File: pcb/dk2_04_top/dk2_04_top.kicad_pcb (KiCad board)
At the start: 2 copper layers, 120 x 108 mm, 112 parts, among them J1 Conn_01x20_Socket, J10 Sync_Out, J11 Euro_Out_2, J12 CV_In_1, J13 CV_In_2, J14 CV_In_3, J15 CV_In_4, J16 Conn_01x05_Pin, J2 Trigger_Out_1, J3 Trigger_Out_2, J4 Sync_In, J5 Euro_Out_1, J6 Micro_SD_Card, J7 Conn_01x16_Socket, J8 Trigger_Out_3, J9 Trigger_Out_4, SW1 SW_Push, SW10 SW_Push, SW11 SW_Push, SW12 SW_Push, SW13 SW_Push, SW14 SW_Push, SW15 SW_Push, SW16 SW_Push, SW17 SW_Push, SW18 SW_Push, SW19 SW_Push, SW2 SW_Push, SW3 SW_Push, SW4 SW_Push, SW5 SW_Push, SW6 SW_Push, SW7 SW_Push, SW8 SW_Push, SW9 SW_Push, U1 74HC595, U10 74HC165, U2 74HC595, U3 CA56-12EWA, U4 74HC165, U5 74HC165, U6 74HC4051, U7 MCP6002-xSN, U8 MCP6002-xSN, U9 74HC4051

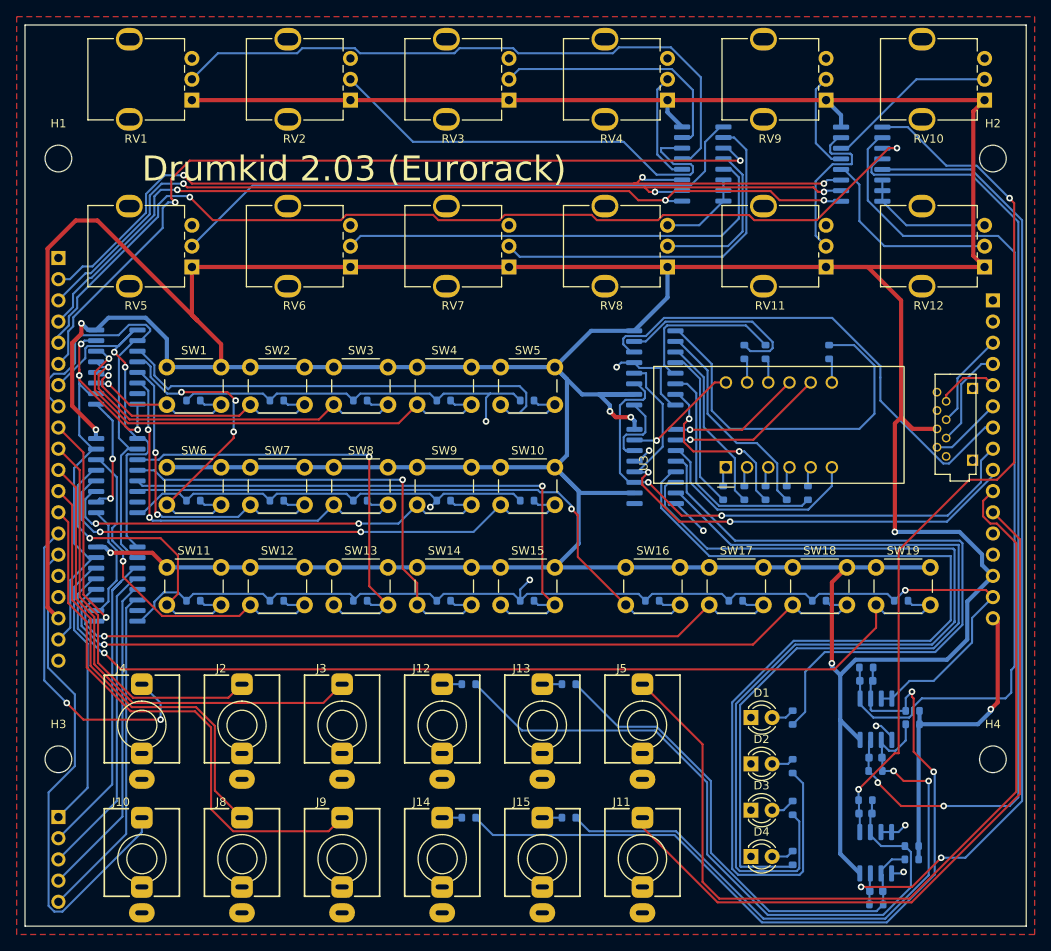
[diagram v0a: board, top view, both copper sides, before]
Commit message: rejigged top board, smaller connectors
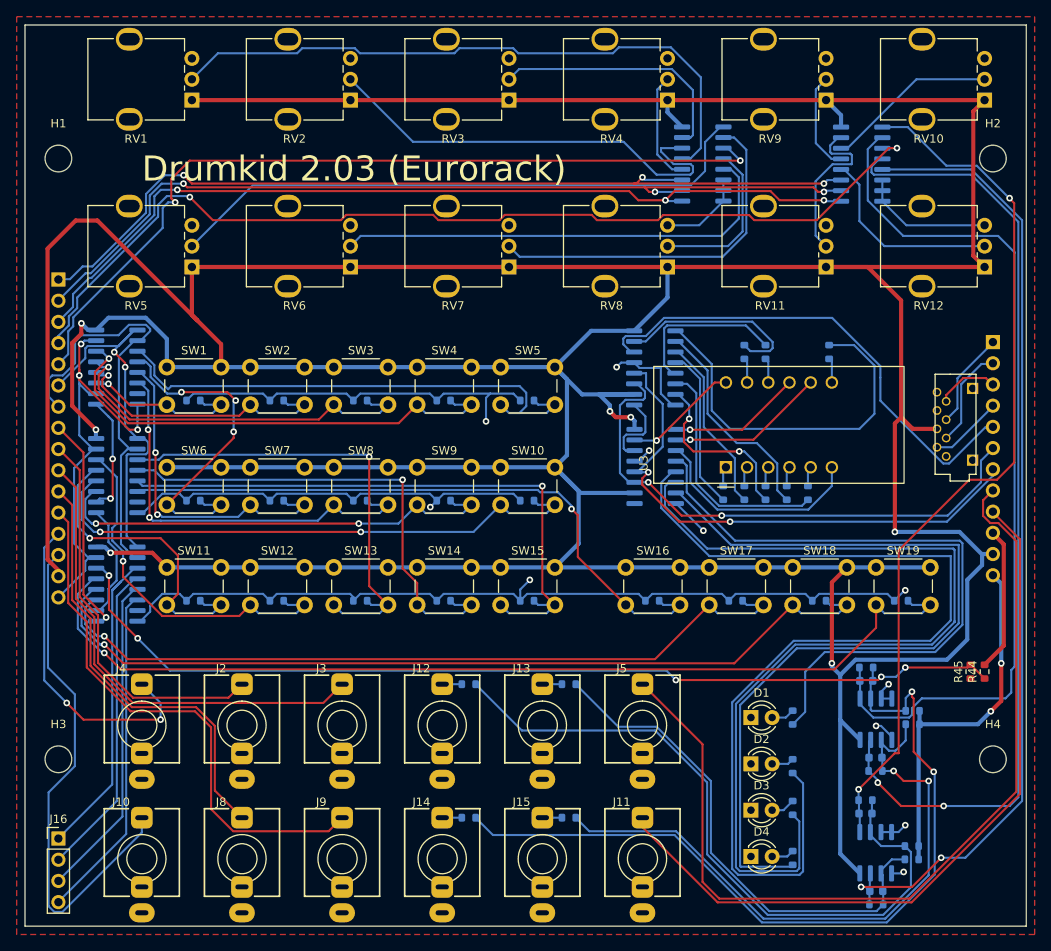
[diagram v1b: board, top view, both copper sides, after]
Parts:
- added R44: 330k, Resistor_SMD:R_0603_1608Metric, F.Cu at (185.0, 117.5)
- added R45: 100k, Resistor_SMD:R_0603_1608Metric, F.Cu at (183.3, 117.5)
- J1: value Conn_01x20_Socket -> Left_Header; footprint Connector_PinSocket_2.54mm:PinSocket_1x20_P2.54mm_Vertical -> Connector_PinHeader_2.54mm:PinHeader_1x16_P2.54mm_Vertical
- J16: value Conn_01x05_Pin -> Conn_01x04_Pin; footprint Connector_PinHeader_2.54mm:PinHeader_1x05_P2.54mm_Vertical -> Connector_PinHeader_2.54mm:PinHeader_1x04_P2.54mm_Vertical; moved to F.Cu
- J7: value Conn_01x16_Socket -> Right_Header; footprint Connector_PinSocket_2.54mm:PinSocket_1x16_P2.54mm_Vertical -> Connector_PinHeader_2.54mm:PinHeader_1x12_P2.54mm_Vertical
- moved J7 5.00 mm to (186.0, 78.0)
- moved J16 2.58 mm to (74.0, 137.5), turned to 0 degrees
- moved J1 2.58 mm to (74.0, 70.5)
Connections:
- J1 pad 1: unconnected-(J1-Pin_1-Pad1) -> 4051_ADDRESS_A
- J1 pad 10: TRIGGER_OUT_1_EURO -> TRIGGER_OUT_2_EURO
- J1 pad 11: TRIGGER_OUT_2_EURO -> TRIGGER_OUT_3_EURO
- J1 pad 12: TRIGGER_OUT_3_EURO -> TRIGGER_OUT_4_EURO
- J1 pad 13: TRIGGER_OUT_4_EURO -> SYNC_IN_EURO
- J1 pad 14: SYNC_IN_EURO -> SYNC_OUT_EURO
- J1 pad 15: SYNC_OUT_EURO -> +3.3V
- J1 pad 16: unconnected-(J1-Pin_16-Pad16) -> GND
- J1 pad 2: 4051_ADDRESS_A -> 4051_ADDRESS_B
- J1 pad 3: 4051_ADDRESS_B -> 4051_ADDRESS_C
- J1 pad 4: 4051_ADDRESS_C -> 4051_READING_1
- J1 pad 5: 4051_READING_1 -> 4051_READING_0
- J1 pad 6: 4051_READING_0 -> 165_LOAD
- J1 pad 7: 165_LOAD -> 165_CLOCK
- J1 pad 8: 165_CLOCK -> 165_DATA
- J1 pad 9: 165_DATA -> TRIGGER_OUT_1_EURO
- J7 pad 1: unconnected-(J7-Pin_1-Pad1) -> SD_CLOCK
- J7 pad 10: EURO_OUT_1 -> +12V
- J7 pad 11: EURO_OUT_2 -> +3.3V
- J7 pad 12: +12V -> -12V
- J7 pad 2: unconnected-(J7-Pin_2-Pad2) -> SD_SERIAL_IN
- J7 pad 3: SD_CLOCK -> SD_SERIAL_OUT
- J7 pad 4: SD_SERIAL_IN -> SD_CHIP_SELECT
- J7 pad 5: SD_SERIAL_OUT -> 595_DATA
- J7 pad 6: SD_CHIP_SELECT -> 595_CLOCK
- J7 pad 7: 595_DATA -> 595_LATCH
- J7 pad 8: 595_CLOCK -> EURO_OUT_1
- J7 pad 9: 595_LATCH -> EURO_OUT_2
- U10 pad 14: Net-(J16-Pin_1) -> 12V DETECTION
- U10 pad 3: Net-(J16-Pin_2) -> Net-(J16-Pin_1)
- U10 pad 4: Net-(J16-Pin_3) -> Net-(J16-Pin_2)
- U10 pad 5: Net-(J16-Pin_4) -> Net-(J16-Pin_3)
- U10 pad 6: Net-(J16-Pin_5) -> Net-(J16-Pin_4)
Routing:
- net 12V DETECTION: track 0.00 -> 115.9 mm, vias 0 -> 5
- net Net-(J16-Pin_5): track 41.0 -> 0.00 mm
- net GND: track 343.4 -> 310.9 mm, vias 13 -> 14
- net +12V: track 0.00 -> 17.2 mm
- net +3.3V: track 734.0 -> 728.5 mm
- net -12V: track 38.8 -> 44.3 mm, vias 1 -> 2
- net Net-(J16-Pin_1): track 33.3 -> 38.0 mm
- net Net-(U10-D0): track 90.6 -> 92.9 mm
- net Net-(J16-Pin_4): track 39.1 -> 41.0 mm
- net Net-(U10-D1): track 103.5 -> 105.3 mm
- net Net-(J16-Pin_3): track 37.8 -> 39.1 mm

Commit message: autosave works
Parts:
- J1: footprint Connector_PinHeader_2.54mm:PinHeader_1x16_P2.54mm_Vertical -> Connector_PinSocket_2.54mm:PinSocket_1x16_P2.54mm_Vertical
- J7: footprint Connector_PinHeader_2.54mm:PinHeader_1x12_P2.54mm_Vertical -> Connector_PinSocket_2.54mm:PinSocket_1x12_P2.54mm_Vertical
- moved RV1 11.2 mm to (80.0, 54.0), turned to 90 degrees
- moved RV10 11.2 mm to (175.0, 54.0), turned to 90 degrees
- moved RV11 11.2 mm to (156.0, 74.0), turned to 90 degrees
- moved RV12 11.2 mm to (175.0, 74.0), turned to 90 degrees
- moved RV2 11.2 mm to (99.0, 54.0), turned to 90 degrees
- moved RV3 11.2 mm to (118.0, 54.0), turned to 90 degrees
- moved RV4 11.2 mm to (137.0, 54.0), turned to 90 degrees
- moved RV5 11.2 mm to (80.0, 74.0), turned to 90 degrees
- moved RV6 11.2 mm to (99.0, 74.0), turned to 90 degrees
- moved RV7 11.2 mm to (118.0, 74.0), turned to 90 degrees
- moved RV8 11.2 mm to (137.0, 74.0), turned to 90 degrees
- moved RV9 11.2 mm to (156.0, 54.0), turned to 90 degrees
- moved U9 2.63 mm to (168.0, 58.0)
- moved U6 2.60 mm to (149.0, 58.0)
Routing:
- net +3.3V: track 728.5 -> 704.9 mm, vias 7 -> 8
- net Net-(U6-A7): track 19.6 -> 36.5 mm, vias 0 -> 2
- net Net-(U6-A4): track 71.6 -> 88.0 mm, vias 0 -> 2
- net Net-(U6-A6): track 43.5 -> 53.4 mm, vias 0 -> 2
- net 4051_ADDRESS_A: track 107.1 -> 115.4 mm, vias 3 -> 2
- net Net-(U9-A1): track 20.6 -> 13.9 mm
- net Net-(U6-A1): track 54.1 -> 47.5 mm, vias 0 -> 1
- net 4051_ADDRESS_B: track 106.2 -> 112.1 mm, vias 3 -> 2
- net Net-(U6-A0): track 76.3 -> 72.0 mm
- net 4051_READING_0: track 100.4 -> 96.2 mm, vias 2 -> 0
- net GND: track 310.9 -> 306.8 mm, vias 14 -> 17
- net Net-(U9-A2): track 19.8 -> 23.2 mm, vias 0 -> 2
- net 4051_READING_1: track 118.6 -> 115.7 mm
- net Net-(U6-A3): track 13.2 -> 10.4 mm
- net Net-(U6-A2): track 30.4 -> 28.0 mm
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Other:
- board text added: "Drumkid 2.04 (Eurorack)"
- board text removed: "Drumkid 2.03 (Eurorack)"
